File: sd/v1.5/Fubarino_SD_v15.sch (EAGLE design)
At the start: 33 parts, among them IC1 PIC32MX440F256H-80I/PT, IC2 MCP1702T-3302E/MB, J1 MICRO_SD_CARD_SOCKET, J2 M28USEPIN1, J3 M28NOPIN1, J8 UX60A-MB-5ST, Q1 8MHz, Q2 32.768 KHz

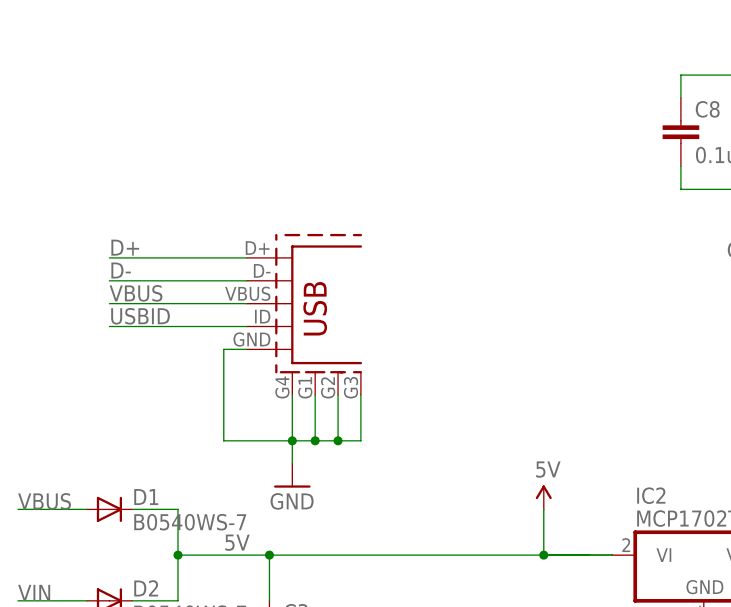
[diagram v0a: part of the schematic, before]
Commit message: Swapped USB connector for Microchip's Hirose.
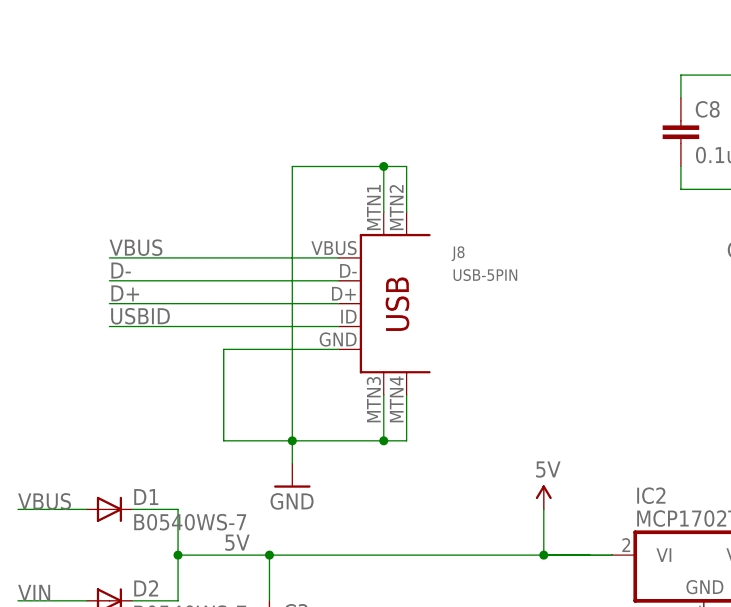
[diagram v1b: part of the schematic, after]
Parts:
- J8: value UX60A-MB-5ST -> USB-5PIN; device SparkFun02-20-08:USB_5PIN -> SchmalzHaus:USB-5PIN
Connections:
- net GND: now also J8.MTN1, J8.MTN2, J8.MTN3, J8.MTN4; no longer J8.P$1, J8.P$2, J8.P$3, J8.SHIELD
- net USBID: now also J8.ID; no longer J8.USB_ID
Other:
- note added: "1/10/2013 - v1.5 (Microchip version)"
- note added: "Added chipKIT to silk Added RX (pin 8) and TX (pin 9) to slik Chaned USB connector to Hirose"
- note removed: "1/10/2013 - v1.5"
- note removed: "Added chipKIT to silk Added RX (pin 8) and TX (pin 9) to slik"
- note removed: "J8"
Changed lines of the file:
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@@
 <?xml version="1.0" encoding="utf-8"?>
 <!DOCTYPE eagle SYSTEM "eagle.dtd">
-<eagle version="6.3">
+<eagle version="6.4">
 <drawing>
 <settings>
@@
 <layer number="122" name="_bsilk" color="7" fill="1" visible="no" active="no"/>
 <layer number="125" name="_tNames" color="7" fill="1" visible="no" active="yes"/>
+<layer number="128" name="128bmp" color="7" fill="1" visible="yes" active="yes"/>
+<layer number="129" name="129bmp" color="7" fill="1" visible="yes" active="yes"/>
+<layer number="130" name="130bmp" color="7" fill="1" visible="yes" active="yes"/>
 <layer number="144" name="Drill_legend" color="7" fill="1" visible="no" active="yes"/>
 <layer number="151" name="HeatSink" color="7" fill="1" visible="no" active="no"/>
+<layer number="199" name="Contour" color="7" fill="1" visible="yes" active="yes"/>
 <layer number="200" name="200bmp" color="1" fill="10" visible="no" active="no"/>
 <layer number="201" name="201bmp" color="2" fill="1" visible="no" active="no"/>
@@
 <part name="GND8" library="SparkFun02-20-08" deviceset="GND" device=""/>
 <part name="FRAME2" library="SparkFun02-20-08" deviceset="FRAME-A3" device=""/>
-<part name="J8" library="SparkFun02-20-08" deviceset="USB_5PIN" device="" value="UX60A-MB-5ST"/>
 <part name="GND20" library="SparkFun02-20-08" deviceset="GND" device=""/>
 <part name="C13" library="SparkFun02-20-08" deviceset="CAP" device="0805" value="10uF"/>
@@
 <part name="D1" library="SparkFun" deviceset="DIODE" device="SOD" value="B0540WS-7"/>
 <part name="D2" library="SparkFun" deviceset="DIODE" device="SOD" value="B0540WS-7"/>
+<part name="J8" library="SchmalzHaus" deviceset="USB-5PIN" device=""/>
 </parts>
 <sheets>
@@
 <plain>
 <text x="137.16" y="27.94" size="1.778" layer="98" rot="R90">Power ON LED</text>
-<text x="40.64" y="91.44" size="1.778" layer="98">USB Function (Mini B)</text>
+<text x="40.64" y="99.06" size="1.778" layer="98">USB Function (Mini B)</text>
 <text x="10.16" y="248.92" size="6.4516" layer="98" ratio="15">Fubarino SD</text>
 <text x="10.16" y="243.84" size="3.81" layer="98" ratio="15">www.fubarino.com/SD</text>
 <text x="10.16" y="238.76" size="1.778" layer="98">Designed by : Brian Schmalz and Rick Anderson</text>
-<text x="58.42" y="81.28" size="1.778" layer="98">J8</text>
 <text x="10.16" y="231.14" size="1.778" layer="98">If you like the Fubarino SD, please consider that</text>
 <text x="10.16" y="228.6" size="1.778" layer="98">SchmalzHaus can design a customized version</text>
@@
 <text x="5.08" y="7.62" size="1.778" layer="98"> software, hardware and materials distributed under this License is distributed on an “AS IS” BASIS, WITHOUT WARRANTIES OR CONDITIONS OF ANY KIND, either express or implied. </text>
 <text x="5.08" y="5.08" size="1.778" layer="98"> See the License for the specific language governing permissions and limitations under the License.</text>
-<text x="10.16" y="165.1" size="1.778" layer="98">1/10/2013 - v1.5</text>
-<text x="12.7" y="160.02" size="1.778" layer="98">Added chipKIT to silk
-Added RX (pin 8) and TX (pin 9) to slik</text>
+<text x="10.16" y="165.1" size="1.778" layer="98">1/10/2013 - v1.5 (Microchip version)</text>
+<text x="12.7" y="157.48" size="1.778" layer="98">Added chipKIT to silk
+Added RX (pin 8) and TX (pin 9) to slik
+Chaned USB connector to Hirose</text>
 </plain>
 <instances>
@@
 <instance part="GND8" gate="1" x="111.76" y="25.4"/>
 <instance part="FRAME2" gate="G$1" x="0" y="0"/>
-<instance part="J8" gate="G$1" x="53.34" y="81.28" smashed="yes"/>
 <instance part="GND20" gate="1" x="48.26" y="25.4"/>
 <instance part="C13" gate="G$1" x="111.76" y="33.02"/>
@@
 <instance part="D1" gate="G$1" x="30.48" y="58.42"/>
 <instance part="D2" gate="G$1" x="30.48" y="48.26"/>
+<instance part="J8" gate="G$1" x="60.96" y="81.28"/>
 </instances>
 <busses>
@@
 </segment>
 <segment>
-<wire x1="43.18" y1="76.2" x2="45.72" y2="76.2" width="0.1524" layer="91"/>
+<wire x1="43.18" y1="76.2" x2="55.88" y2="76.2" width="0.1524" layer="91"/>
 <wire x1="43.18" y1="76.2" x2="43.18" y2="66.04" width="0.1524" layer="91"/>
 <wire x1="43.18" y1="66.04" x2="50.8" y2="66.04" width="0.1524" layer="91"/>
-<wire x1="50.8" y1="66.04" x2="50.8" y2="71.12" width="0.1524" layer="91"/>
-<wire x1="50.8" y1="66.04" x2="53.34" y2="66.04" width="0.1524" layer="91"/>
-<wire x1="53.34" y1="66.04" x2="53.34" y2="71.12" width="0.1524" layer="91"/>
-<wire x1="53.34" y1="66.04" x2="55.88" y2="66.04" width="0.1524" layer="91"/>
-<wire x1="55.88" y1="66.04" x2="55.88" y2="71.12" width="0.1524" layer="91"/>
-<wire x1="55.88" y1="66.04" x2="58.42" y2="66.04" width="0.1524" layer="91"/>
-<wire x1="58.42" y1="66.04" x2="58.42" y2="71.12" width="0.1524" layer="91"/>
 <wire x1="50.8" y1="66.04" x2="50.8" y2="63.5" width="0.1524" layer="91"/>
+<pinref part="GND2" gate="1" pin="GND"/>
+<pinref part="J8" gate="G$1" pin="GND"/>
+<pinref part="J8" gate="G$1" pin="MTN3"/>
+<wire x1="50.8" y1="66.04" x2="60.96" y2="66.04" width="0.1524" layer="91"/>
+<wire x1="60.96" y1="66.04" x2="60.96" y2="71.12" width="0.1524" layer="91"/>
 <junction x="50.8" y="66.04"/>
-<junction x="53.34" y="66.04"/>
-<junction x="55.88" y="66.04"/>
-<pinref part="J8" gate="G$1" pin="SHIELD"/>
-<pinref part="J8" gate="G$1" pin="P$1"/>
-<pinref part="J8" gate="G$1" pin="P$2"/>
-<pinref part="J8" gate="G$1" pin="P$3"/>
-<pinref part="J8" gate="G$1" pin="GND"/>
-<pinref part="GND2" gate="1" pin="GND"/>
+<pinref part="J8" gate="G$1" pin="MTN4"/>
+<wire x1="60.96" y1="66.04" x2="63.5" y2="66.04" width="0.1524" layer="91"/>
+<wire x1="63.5" y1="66.04" x2="63.5" y2="71.12" width="0.1524" layer="91"/>
+<junction x="60.96" y="66.04"/>
+<wire x1="50.8" y1="66.04" x2="50.8" y2="96.52" width="0.1524" layer="91"/>
+<pinref part="J8" gate="G$1" pin="MTN1"/>
+<wire x1="50.8" y1="96.52" x2="60.96" y2="96.52" width="0.1524" layer="91"/>
+<wire x1="60.96" y1="96.52" x2="60.96" y2="91.44" width="0.1524" layer="91"/>
+<pinref part="J8" gate="G$1" pin="MTN2"/>
+<wire x1="60.96" y1="96.52" x2="63.5" y2="96.52" width="0.1524" layer="91"/>
+<wire x1="63.5" y1="96.52" x2="63.5" y2="91.44" width="0.1524" layer="91"/>
+<junction x="60.96" y="96.52"/>
 </segment>
 <segment>
@@
 </segment>
 <segment>
-<wire x1="45.72" y1="86.36" x2="30.48" y2="86.36" width="0.1524" layer="91"/>
-<label x="30.48" y="86.614" size="1.778" layer="95"/>
+<wire x1="55.88" y1="81.28" x2="30.48" y2="81.28" width="0.1524" layer="91"/>
+<label x="30.48" y="81.534" size="1.778" layer="95"/>
 <pinref part="J8" gate="G$1" pin="D+"/>
 </segment>
@@
 </segment>
 <segment>
-<wire x1="45.72" y1="83.82" x2="30.48" y2="83.82" width="0.1524" layer="91"/>
 <label x="30.48" y="84.074" size="1.778" layer="95"/>
 <pinref part="J8" gate="G$1" pin="D-"/>
+<wire x1="30.48" y1="83.82" x2="55.88" y2="83.82" width="0.1524" layer="91"/>
 </segment>
 </net>
 <net name="VBUS" class="0">
 <segment>
-<wire x1="45.72" y1="81.28" x2="30.48" y2="81.28" width="0.1524" layer="91"/>
-<label x="30.48" y="81.534" size="1.778" layer="95"/>
+<label x="30.48" y="86.614" size="1.778" layer="95"/>
+<wire x1="30.48" y1="86.36" x2="55.88" y2="86.36" width="0.1524" layer="91"/>
 <pinref part="J8" gate="G$1" pin="VBUS"/>
 </segment>
@@
 </segment>
 <segment>
-<wire x1="45.72" y1="78.74" x2="30.48" y2="78.74" width="0.1524" layer="91"/>
 <label x="30.48" y="78.994" size="1.778" layer="95"/>
-<pinref part="J8" gate="G$1" pin="USB_ID"/>
-</segment>
-</net>
+<pinref part="J8" gate="G$1" pin="ID"/>
+<wire x1="30.48" y1="78.74" x2="55.88" y2="78.74" width="0.1524" layer="91"/>
+</segment>
+</net>

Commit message: Updated Fubarino SD v1.5 board with CE, RoHS, chipKIT on silk, updated BOM, rendered top and bottom from gerbers.
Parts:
- added U$2: CE_MARK5MM, SchmalzHausPublic:CE_MARK5MM
- added U$3: ROHS_GARBAGE, SchmalzHausPublic:ROHS_GARBAGE
- added U$4, U$5: CHIPKIT2MM, SchmalzHausPublic:CHIPKIT2MM
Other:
- note added: "2/26/2013 - v1.5 (Microchip version)"
- note added: "Added chipKIT, CE, RoSH to silk Added RX (pin 8) and TX (pin 9) to slik Chaned USB connector to Hirose"
- note added: "Designed by : Brian Schmalz (Schmalz Haus LLC) and Rick Anderson (FUBARLabs)"
- note added: "PIC32MX795F512H-80I/PT (alt)"
- note removed: "1/10/2013 - v1.5 (Microchip version)"
- note removed: "Added chipKIT to silk Added RX (pin 8) and TX (pin 9) to slik Chaned USB connector to Hirose"
- note removed: "Designed by : Brian Schmalz and Rick Anderson"
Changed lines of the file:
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@@
 <part name="D2" library="SparkFun" deviceset="DIODE" device="SOD" value="B0540WS-7"/>
 <part name="J8" library="SchmalzHaus" deviceset="USB-5PIN" device=""/>
+<part name="U$2" library="SchmalzHausPublic" deviceset="CE_MARK" device="5MM"/>
+<part name="U$3" library="SchmalzHausPublic" deviceset="ROHS_GARBAGE" device=""/>
+<part name="U$4" library="SchmalzHausPublic" deviceset="CHIPKIT" device="2MM"/>
+<part name="U$5" library="SchmalzHausPublic" deviceset="CHIPKIT" device="2MM"/>
 </parts>
 <sheets>
@@
 <text x="10.16" y="248.92" size="6.4516" layer="98" ratio="15">Fubarino SD</text>
 <text x="10.16" y="243.84" size="3.81" layer="98" ratio="15">www.fubarino.com/SD</text>
-<text x="10.16" y="238.76" size="1.778" layer="98">Designed by : Brian Schmalz and Rick Anderson</text>
+<text x="10.16" y="238.76" size="1.778" layer="98">Designed by : Brian Schmalz (Schmalz Haus LLC) and Rick Anderson (FUBARLabs)</text>
 <text x="10.16" y="231.14" size="1.778" layer="98">If you like the Fubarino SD, please consider that</text>
 <text x="10.16" y="228.6" size="1.778" layer="98">SchmalzHaus can design a customized version</text>
@@
 <text x="5.08" y="7.62" size="1.778" layer="98"> software, hardware and materials distributed under this License is distributed on an “AS IS” BASIS, WITHOUT WARRANTIES OR CONDITIONS OF ANY KIND, either express or implied. </text>
 <text x="5.08" y="5.08" size="1.778" layer="98"> See the License for the specific language governing permissions and limitations under the License.</text>
-<text x="10.16" y="165.1" size="1.778" layer="98">1/10/2013 - v1.5 (Microchip version)</text>
-<text x="12.7" y="157.48" size="1.778" layer="98">Added chipKIT to silk
+<text x="10.16" y="165.1" size="1.778" layer="98">2/26/2013 - v1.5 (Microchip version)</text>
+<text x="12.7" y="157.48" size="1.778" layer="98">Added chipKIT, CE, RoSH to silk
 Added RX (pin 8) and TX (pin 9) to slik
 Chaned USB connector to Hirose</text>
+<text x="88.9" y="121.92" size="1.778" layer="98">PIC32MX795F512H-80I/PT (alt)</text>
 </plain>
 <instances>
@@
 <instance part="D2" gate="G$1" x="30.48" y="48.26"/>
 <instance part="J8" gate="G$1" x="60.96" y="81.28"/>
+<instance part="U$2" gate="G$1" x="241.3" y="12.7"/>
+<instance part="U$3" gate="G$1" x="236.22" y="10.16"/>
+<instance part="U$4" gate="G$1" x="241.3" y="15.24"/>
+<instance part="U$5" gate="G$1" x="241.3" y="17.78"/>
 </instances>
 <busses>
